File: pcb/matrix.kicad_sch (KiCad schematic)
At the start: 136 parts

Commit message: prod plates and db, pcb BOM
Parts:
- D1, D10, D11, D12, D13, D14, D15, D16, D17, D18, D19, D2, D20, D21, D22, D23, D24, D25, D26, D27, D28, D29, D3, D30, D31, D32, D33, D34, D35, D36, D37, D38, D39, D4, D40, D41, D42, D43, D44, D45, D46, D47, D48, D49, D5, D50, D51, D52, D53, D54, D55, D56, D57, D58, D59, D6, D60, D61, D62, D63, D7, D8, D9: LCSC (none) -> C81598; LCSC Part # C81598 -> (none)
- MX1, MX10, MX11, MX12, MX13, MX14, MX15, MX16, MX17, MX18, MX19, MX2, MX20, MX21, MX22, MX23, MX24, MX25, MX26, MX27, MX28, MX29, MX3, MX30, MX31, MX32, MX33, MX34, MX35, MX36, MX37, MX38, MX39, MX4, MX40, MX41, MX42, MX43, MX44, MX45, MX46, MX47, MX48, MX49, MX5, MX50, MX51, MX52, MX53, MX54, MX55, MX56, MX57, MX58, MX59, MX6, MX60, MX61, MX62, MX63, MX64, MX65, MX66, MX67, MX68, MX69, MX7, MX70, MX71, MX72, MX73, MX8, MX9: DNP (none) -> DNP

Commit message: first attempt
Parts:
- removed MX45: 2.25u, MX_Only:MXOnly-2.25U-NoLED, symbol bakeneko-60-pcb-rescue:SW_SPST-Switch
- removed MX58: 2.75u, MX_Only:MXOnly-2.75U-NoLED, symbol bakeneko-60-pcb-rescue:SW_SPST-Switch
- removed MX62: 6.25u, MX_Only:MXOnly-6.25U-ReversedStabilizers-NoLED, symbol bakeneko-60-pcb-rescue:SW_SPST-Switch
- added D64: 1N4148, Diode_SMD:D_SOD-123, symbol bakeneko-60-pcb-rescue:D-Device
- MX16: value 2u -> 1.25u; footprint MX_Only:MXOnly-2U-NoLED -> MX_Only:MXOnly-1.25U-NoLED
- MX32: value 1.75u -> 1u; footprint MX_Only:MXOnly-1.75U-NoLED -> MX_Only:MXOnly-1U-NoLED
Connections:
- net COL0: now also MX16.2 (B); no longer MX32.2 (B)
- net COL1: now also MX32.2 (B)
- net COL14: no longer MX16.2 (B)
- net ROW3: now also D64.1 (K)
- net at D30.2 (A), MX31.1 (A): no longer MX32.1 (A)
- net at D15.2 (A), MX15.1 (A): no longer MX16.1 (A)
- net at D43.2 (A): now also MX16.1 (A)
- new net: D64.2 (A), MX32.1 (A)

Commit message: first round off to fab for quote
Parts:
- removed MX61: 1.25u, MX_Only:MXOnly-1.25U-NoLED, symbol bakeneko-60-pcb-rescue:SW_SPST-Switch
- added MX45: 2u, MX_Only:MXOnly-2U-NoLED, symbol bakeneko-60-pcb-rescue:SW_SPST-Switch
- added MX58: 2.25u, MX_Only:MXOnly-2.25U-NoLED, symbol bakeneko-60-pcb-rescue:SW_SPST-Switch
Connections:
- net COL0: now also MX58.2 (B)
- net COL14: now also MX45.2 (B)
- net at D43.2 (A), MX16.1 (A): now also MX58.1 (A)
- net at D15.2 (A), MX15.1 (A): now also MX45.1 (A)
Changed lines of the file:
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@@
   (junction (at 213.36 92.71) (diameter 0) (color 0 0 0 0)
   )
-  (junction (at 171.45 57.15) (diameter 0) (color 0 0 0 0)
+  (junction (at 55.88 92.71) (diameter 0) (color 0 0 0 0)
   )
-  (junction (at 83.82 110.49) (diameter 0) (color 0 0 0 0)
+  (junction (at 171.45 57.15) (diameter 0) (color 0 0 0 0)
   )
   (junction (at 125.73 82.55) (diameter 0) (color 0 0 0 0)
@@
   (junction (at 59.69 39.37) (diameter 0) (color 0 0 0 0)
   )
+  (junction (at 241.3 31.115) (diameter 0) (color 0 0 0 0)
+  )
   (junction (at 129.54 92.71) (diameter 0) (color 0 0 0 0)
   )
@@
   (junction (at 157.48 39.37) (diameter 0) (color 0 0 0 0)
   )
-  (junction (at 73.66 110.49) (diameter 0) (color 0 0 0 0)
-  )
   (junction (at 209.55 110.49) (diameter 0) (color 0 0 0 0)
   )
@@
   (junction (at 55.88 110.49) (diameter 0) (color 0 0 0 0)
   )
+  (junction (at 251.46 39.37) (diameter 0) (color 0 0 0 0)
+  )
   (junction (at 185.42 39.37) (diameter 0) (color 0 0 0 0)
   )
@@
     (stroke (width 0) (type default) (color 0 0 0 0))
   )
+  (wire (pts (xy 33.655 92.71) (xy 45.72 92.71))
+    (stroke (width 0) (type default) (color 0 0 0 0))
+  )
+  (wire (pts (xy 251.46 31.115) (xy 251.46 39.37))
+    (stroke (width 0) (type default) (color 0 0 0 0))
+  )
   (wire (pts (xy 87.63 74.93) (xy 87.63 57.15))
     (stroke (width 0) (type default) (color 0 0 0 0))
@@
     (stroke (width 0) (type default) (color 0 0 0 0))
   )
-  (wire (pts (xy 73.66 129.54) (xy 73.66 110.49))
-    (stroke (width 0) (type default) (color 0 0 0 0))
-  )
   (wire (pts (xy 213.36 92.71) (xy 213.36 110.49))
     (stroke (width 0) (type default) (color 0 0 0 0))
@@
     (stroke (width 0) (type default) (color 0 0 0 0))
   )
+  (wire (pts (xy 33.655 87.63) (xy 33.655 92.71))
+    (stroke (width 0) (type default) (color 0 0 0 0))
+  )
   (wire (pts (xy 115.57 74.93) (xy 115.57 57.15))
     (stroke (width 0) (type default) (color 0 0 0 0))
   )
+  (wire (pts (xy 241.3 31.115) (xy 241.3 39.37))
+    (stroke (width 0) (type default) (color 0 0 0 0))
+  )
   (wire (pts (xy 195.58 46.99) (xy 181.61 46.99))
     (stroke (width 0) (type default) (color 0 0 0 0))
@@
     (stroke (width 0) (type default) (color 0 0 0 0))
   )
+  (wire (pts (xy 55.88 87.63) (xy 55.88 92.71))
+    (stroke (width 0) (type default) (color 0 0 0 0))
+  )
   (wire (pts (xy 223.52 110.49) (xy 226.06 110.49))
     (stroke (width 0) (type default) (color 0 0 0 0))
@@
     (stroke (width 0) (type default) (color 0 0 0 0))
   )
+  (wire (pts (xy 43.815 87.63) (xy 55.88 87.63))
+    (stroke (width 0) (type default) (color 0 0 0 0))
+  )
   (wire (pts (xy 69.85 64.77) (xy 83.82 64.77))
     (stroke (width 0) (type default) (color 0 0 0 0))
@@
     (stroke (width 0) (type default) (color 0 0 0 0))
   )
-  (wire (pts (xy 241.3 24.13) (xy 241.3 39.37))
+  (wire (pts (xy 241.3 24.13) (xy 241.3 31.115))
     (stroke (width 0) (type default) (color 0 0 0 0))
   )
@@
     (stroke (width 0) (type default) (color 0 0 0 0))
   )
-  (wire (pts (xy 73.66 92.71) (xy 73.66 110.49))
+  (wire (pts (xy 73.66 92.71) (xy 73.66 129.54))
     (stroke (width 0) (type default) (color 0 0 0 0))
   )
@@
     (pin "2")
   )
-  (symbol (lib_id "bakeneko-60-pcb-rescue:SW_SPST-Switch") (at 78.74 110.49 0) (mirror y) (unit 1)
-    (in_bom yes) (on_board yes)
-    (property "Reference" "MX61" (id 0) (at 78.74 104.521 0))
-    (property "Value" "1.25u" (id 1) (at 78.74 106.8324 0))
-    (property "Footprint" "MX_Only:MXOnly-1.25U-NoLED" (id 2) (at 78.74 110.49 0)
-      (effects (font (size 1.27 1.27)) hide)
-    )
-    (property "Datasheet" "~" (id 3) (at 78.74 110.49 0)
-      (effects (font (size 1.27 1.27)) hide)
-    )
-    (property "DNP" "DNP" (id 4) (at 78.74 110.49 0)
-      (effects (font (size 1.27 1.27)) hide)
-    )
-    (pin "1")
-    (pin "2")
-  )
   (symbol (lib_id "bakeneko-60-pcb-rescue:D-Device") (at 69.85 114.3 90) (unit 1)
     (in_bom yes) (on_board yes)
@@
       (effects (font (size 1.27 1.27)) hide)
     )
+    (pin "1")
+    (pin "2")
+  )
+  (symbol (lib_id "bakeneko-60-pcb-rescue:SW_SPST-Switch") (at 246.38 31.115 0) (mirror y) (unit 1)
+    (in_bom yes) (on_board yes)
+    (property "Reference" "MX45" (id 0) (at 250.825 27.94 0))
+    (property "Value" "2u" (id 1) (at 250.825 29.845 0))
+    (property "Footprint" "MX_Only:MXOnly-2U-NoLED" (id 2) (at 246.38 31.115 0)
+      (effects (font (size 1.27 1.27)) hide)
+    )
+    (property "Datasheet" "~" (id 3) (at 246.38 31.115 0)
+      (effects (font (size 1.27 1.27)) hide)
+    )
+    (property "DNP" "DNP" (id 4) (at 246.38 31.115 0)
+      (effects (font (size 1.27 1.27)) hide)
+    )
+    (pin "1")
+    (pin "2")
+  )
+  (symbol (lib_id "bakeneko-60-pcb-rescue:SW_SPST-Switch") (at 38.735 87.63 0) (mirror y) (unit 1)
+    (in_bom yes) (on_board yes)
+    (property "Reference" "MX58" (id 0) (at 38.735 89.535 0))
+    (property "Value" "2.25u" (id 1) (at 38.735 91.44 0))
+    (property "Footprint" "MX_Only:MXOnly-2.25U-NoLED" (id 2) (at 38.735 87.63 0)
+      (effects (font (size 1.27 1.27)) hide)
+    )
+    (property "Datasheet" "~" (id 3) (at 38.735 87.63 0)
+      (effects (font (size 1.27 1.27)) hide)
+    )
+    (property "DNP" "DNP" (id 4) (at 38.735 87.63 0)
+      (effects (font (size 1.27 1.27)) hide)
+    )

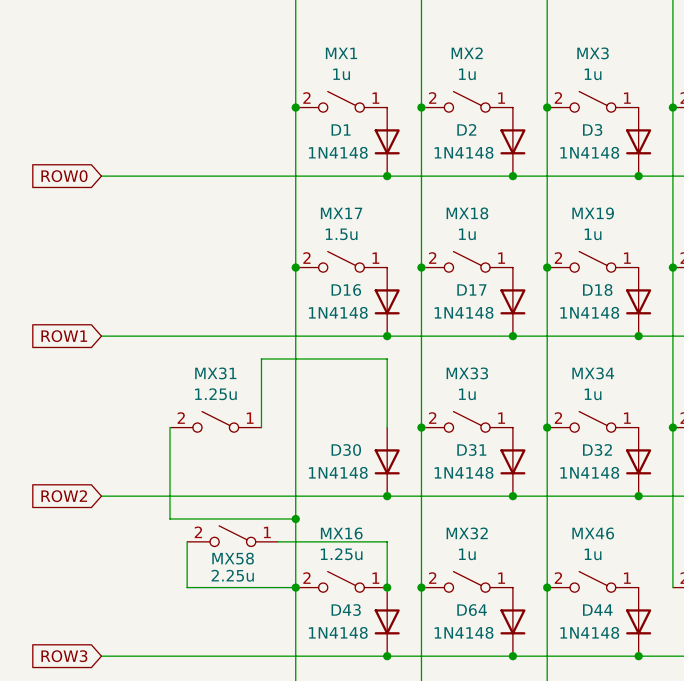
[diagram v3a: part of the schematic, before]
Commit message: more connector movement, add split bs
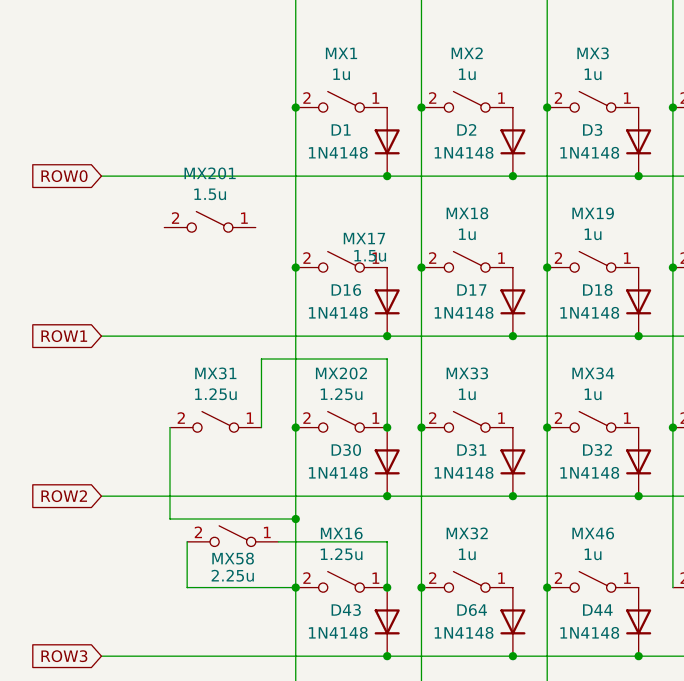
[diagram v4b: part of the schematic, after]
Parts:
- added MX201: 1.5u, MX_Only:MXOnly-1.5U-NoLED, symbol bakeneko-60-pcb-rescue:SW_SPST-Switch
- added MX202: 1.25u, MX_Only:MXOnly-1.25U-NoLED, symbol bakeneko-60-pcb-rescue:SW_SPST-Switch
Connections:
- net COL0: now also MX202.2 (B)
- net at D30.2 (A), MX31.1 (A): now also MX202.1 (A)
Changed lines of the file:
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@@
   (junction (at 97.79 82.55) (diameter 0) (color 0 0 0 0)
   )
+  (junction (at 45.72 74.93) (diameter 0) (color 0 0 0 0)
+  )
   (junction (at 73.66 92.71) (diameter 0) (color 0 0 0 0)
   )
@@
   (junction (at 251.46 39.37) (diameter 0) (color 0 0 0 0)
   )
+  (junction (at 55.88 74.93) (diameter 0) (color 0 0 0 0)
+  )
   (junction (at 185.42 39.37) (diameter 0) (color 0 0 0 0)
   )
@@
     (stroke (width 0) (type default) (color 0 0 0 0))
   )
-  (wire (pts (xy 45.72 57.15) (xy 45.72 85.09))
+  (wire (pts (xy 45.72 57.15) (xy 45.72 74.93))
     (stroke (width 0) (type default) (color 0 0 0 0))
   )
@@
     (stroke (width 0) (type default) (color 0 0 0 0))
   )
+  (wire (pts (xy 45.72 74.93) (xy 45.72 85.09))
+    (stroke (width 0) (type default) (color 0 0 0 0))
+  )
   (wire (pts (xy 55.88 87.63) (xy 55.88 92.71))
     (stroke (width 0) (type default) (color 0 0 0 0))
@@
   (symbol (lib_id "bakeneko-60-pcb-rescue:SW_SPST-Switch") (at 50.8 57.15 0) (mirror y) (unit 1)
     (in_bom yes) (on_board yes)
-    (property "Reference" "MX17" (id 0) (at 50.8 51.181 0))
-    (property "Value" "1.5u" (id 1) (at 50.8 53.4924 0))
+    (property "Reference" "MX17" (id 0) (at 53.34 53.975 0))
+    (property "Value" "1.5u" (id 1) (at 53.975 55.88 0))
     (property "Footprint" "MX_Only:MXOnly-1.5U-NoLED" (id 2) (at 50.8 57.15 0)
       (effects (font (size 1.27 1.27)) hide)
@@
     (pin "2")
   )
+  (symbol (lib_id "bakeneko-60-pcb-rescue:SW_SPST-Switch") (at 50.8 74.93 0) (mirror y) (unit 1)
+    (in_bom yes) (on_board yes)
+    (property "Reference" "MX202" (id 0) (at 50.8 68.961 0))
+    (property "Value" "1.25u" (id 1) (at 50.8 71.2724 0))
+    (property "Footprint" "MX_Only:MXOnly-1.25U-NoLED" (id 2) (at 50.8 74.93 0)
+      (effects (font (size 1.27 1.27)) hide)
+    )
+    (property "Datasheet" "~" (id 3) (at 50.8 74.93 0)
+      (effects (font (size 1.27 1.27)) hide)
+    )
+    (property "DNP" "DNP" (id 4) (at 50.8 74.93 0)
+      (effects (font (size 1.27 1.27)) hide)
+    )
+    (pin "1")
+    (pin "2")
+  )
   (symbol (lib_id "bakeneko-60-pcb-rescue:SW_SPST-Switch") (at 38.735 87.63 0) (mirror y) (unit 1)
     (in_bom yes) (on_board yes)
@@
       (effects (font (size 1.27 1.27)) hide)
     )
+    (pin "1")
+    (pin "2")
+  )
+  (symbol (lib_id "bakeneko-60-pcb-rescue:SW_SPST-Switch") (at 36.195 52.705 0) (mirror y) (unit 1)
+    (in_bom yes) (on_board yes)
+    (property "Reference" "MX201" (id 0) (at 36.195 46.736 0))
+    (property "Value" "1.5u" (id 1) (at 36.195 49.0474 0))
+    (property "Footprint" "MX_Only:MXOnly-1.5U-NoLED" (id 2) (at 36.195 52.705 0)
+      (effects (font (size 1.27 1.27)) hide)
+    )
+    (property "Datasheet" "~" (id 3) (at 36.195 52.705 0)
+      (effects (font (size 1.27 1.27)) hide)
+    )
+    (property "DNP" "DNP" (id 4) (at 36.195 52.705 0)
+      (effects (font (size 1.27 1.27)) hide)
+    )

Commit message: final?
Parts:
- removed D60: 1N4148, Diode_SMD:D_SOD-123, symbol bakeneko-60-pcb-rescue:D-Device
- removed MX201: 1.5u, MX_Only:MXOnly-1.5U-NoLED, symbol bakeneko-60-pcb-rescue:SW_SPST-Switch
- removed MX59, MX60, MX63, MX64, MX65, MX66: 1.25u, MX_Only:MXOnly-1.25U-NoLED, symbol bakeneko-60-pcb-rescue:SW_SPST-Switch
